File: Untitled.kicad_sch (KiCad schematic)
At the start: 20 parts, among them J1 Battery Connector, J2 Top Screw Terminal, J3 Bottom Screw Terminal, Q1 Q_NMOS_DGS, Q2 Q_NMOS_DGS, Q3 Q_NMOS_DGS, U1 XIAO-ESP32-S3-SMD, U3 LSM6DSO32, U4 MS5611-01BA

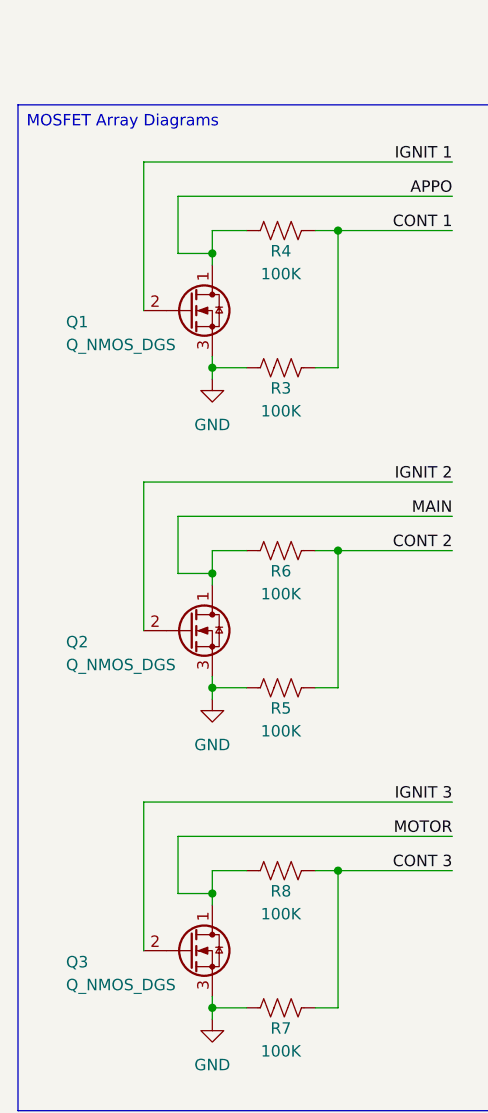
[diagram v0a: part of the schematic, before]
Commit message: New Rgs Resistors and Ground Pour
Added a set of 3 new resistors that bridge the gate of the MOSFETs to ground with a 4.7 ohm resistor, which can help filter out any unintentional activation of the MOSFET due to interference (detailed in datasheet). Also added a ground pour to the PCB for added EMI resistance and overall higher performance.
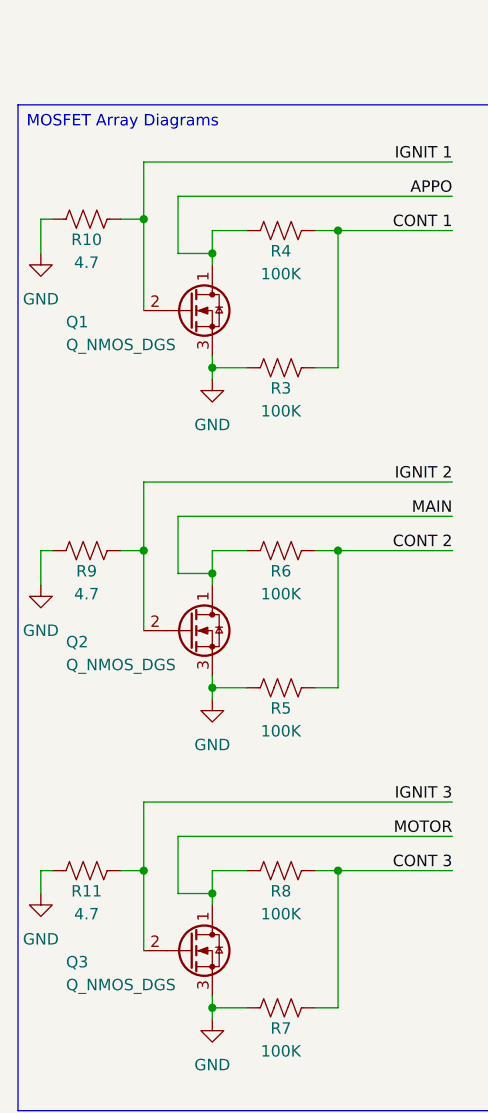
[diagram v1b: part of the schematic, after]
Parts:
- added R10, R11, R9: 4.7, Resistor_SMD:R_0402_1005Metric, symbol Device:R_US
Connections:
- net -BATT: now also R10.2, R11.2, R9.2
- net IGNIT 1: now also R10.1
- net IGNIT 2: now also R9.1
- net IGNIT 3: now also R11.1
